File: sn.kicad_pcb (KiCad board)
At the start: 2 copper layers, 70.5 x 74.3 mm, 47 parts, among them J1 220V, J2 Load, J3 USB_C_Receptacle_USB2.0_16P, J4 Conn_02x03, Q1 BTB16-600B, Q2 BC847B, SW1 RESET, SW2 BOOT, U1 LTV-814, U2 ESP32-S3-WROOM-1, U3 MOC3052M, U5 USBLC6-2SC6, U6 LM1117MP-3.3

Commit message: redesing pcb
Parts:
- moved H3 10.5 mm to (90.8, 42.5)
- moved J1 10.2 mm to (82.5, 43.2)
- moved C7 0.28 mm to (32.0, 40.1)
- moved C8 0.28 mm to (30.1, 40.1)
- moved R7 0.19 mm to (37.7, 59.7)
- turned R2 to 0 degrees
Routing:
- net GND: track 268.2 -> 25.2 mm, vias 91 -> 77
- net Net-(J2-Pin_2): track 95.9 -> 81.0 mm, vias 0 -> 2
- net /AC_N: track 90.8 -> 78.0 mm
- net /AC_L: track 141.1 -> 135.1 mm
- removed copper zone on B.Cu, net /AC_L

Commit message: add ASM
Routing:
- net /AC_N: track 78.0 -> 74.2 mm
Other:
- board text added: "Вікторія Михайлова Група ТРМ-12"

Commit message: remove l1 l2 d4 d2
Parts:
- removed D2, D4: ESD3.3, Diode_SMD:D_SOD-923
- removed L1, L2: 220Ohm, PCM_SparkFun-Capacitor:C_0603_1608Metric
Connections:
- D3 pad 2: Net-(D3-A) -> Net-(C2-+)
- F1 pad 2: Net-(F1-Pad2) -> Net-(D1-A)
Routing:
- net Net-(C2-+): track 63.3 -> 69.5 mm
- net Net-(D3-A): track 4.94 -> 0.00 mm
- net Net-(D1-A): track 4.81 -> 9.08 mm
- net Net-(F1-Pad2): track 2.54 -> 0.00 mm
- net /ESP_IO0: track 38.3 -> 35.9 mm

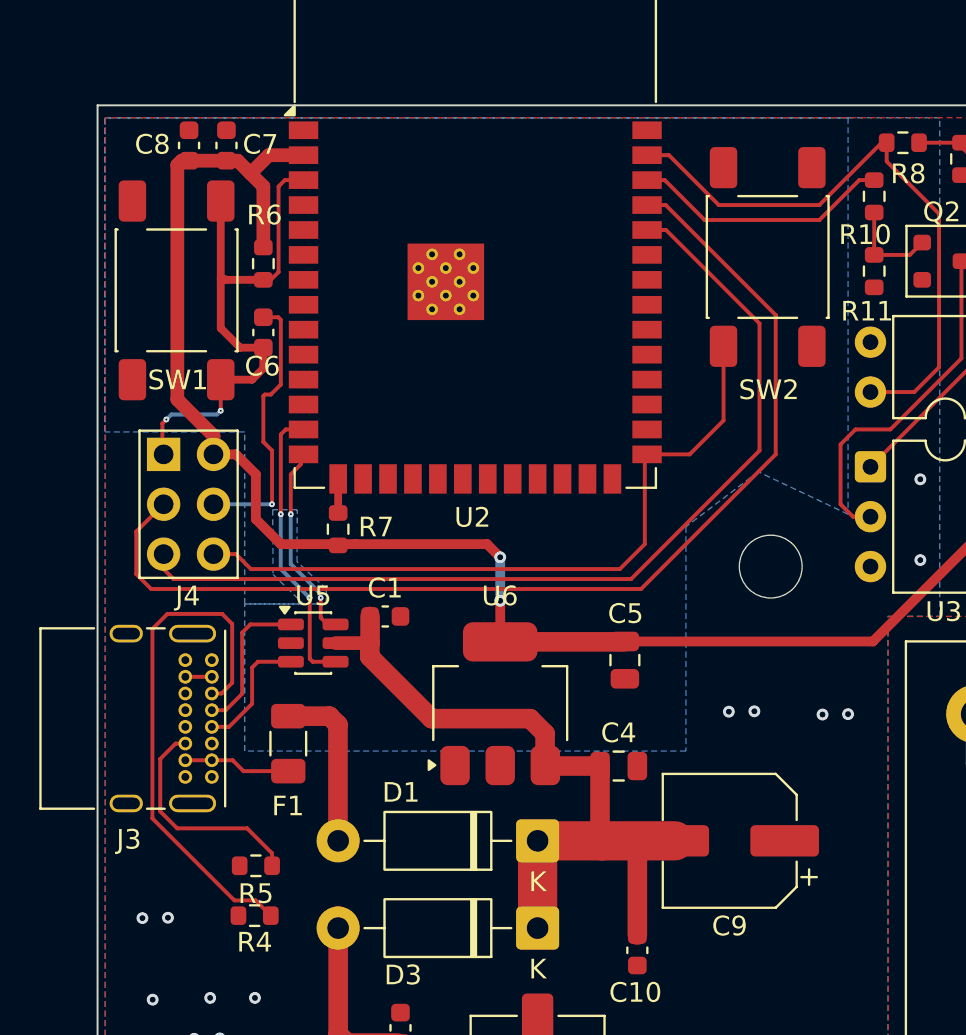
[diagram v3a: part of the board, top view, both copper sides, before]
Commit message: return tht type-c
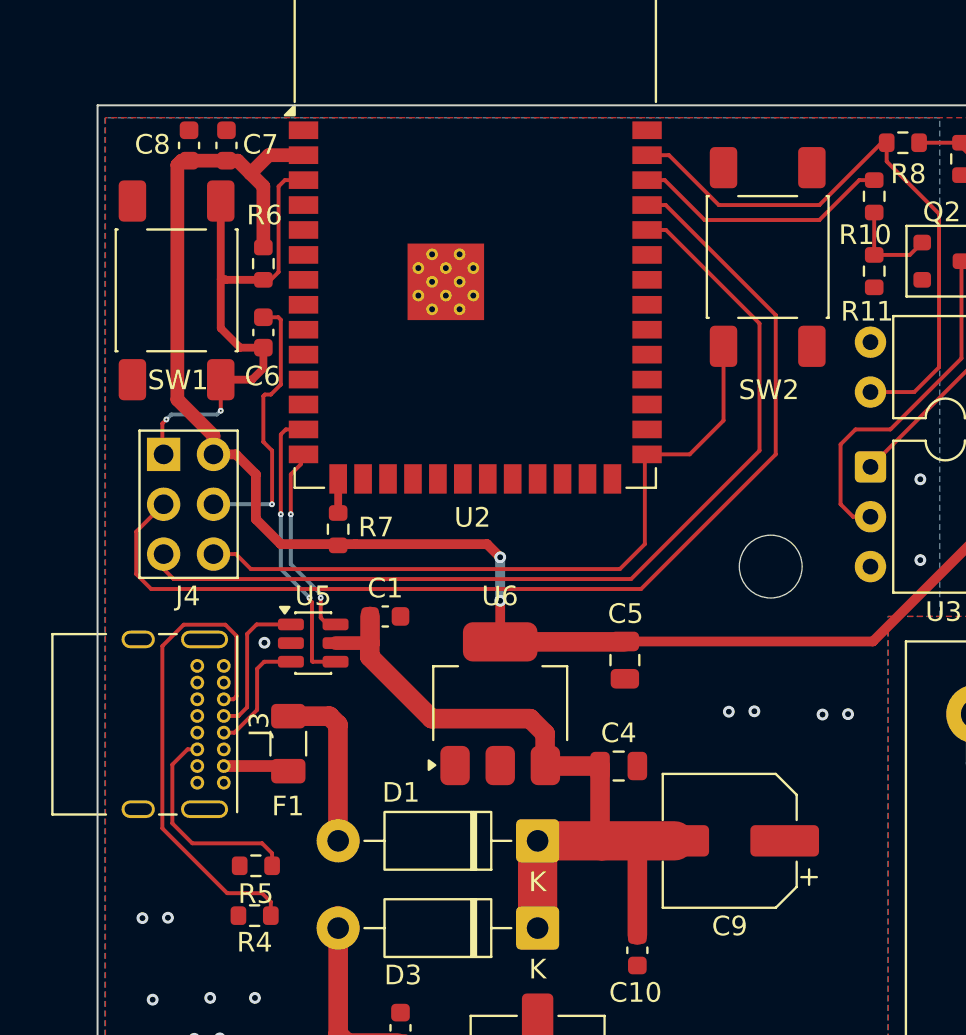
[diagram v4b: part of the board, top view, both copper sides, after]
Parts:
- moved J3 0.68 mm to (31.8, 66.7)
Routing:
- net Net-(F1-Pad1): track 6.97 -> 3.89 mm
- net /CC1: track 26.6 -> 25.3 mm
- net GND: track 25.2 -> 24.2 mm, vias 77 -> 78
- net /CC2: track 11.5 -> 10.9 mm
- net /D-: track 6.65 -> 6.14 mm

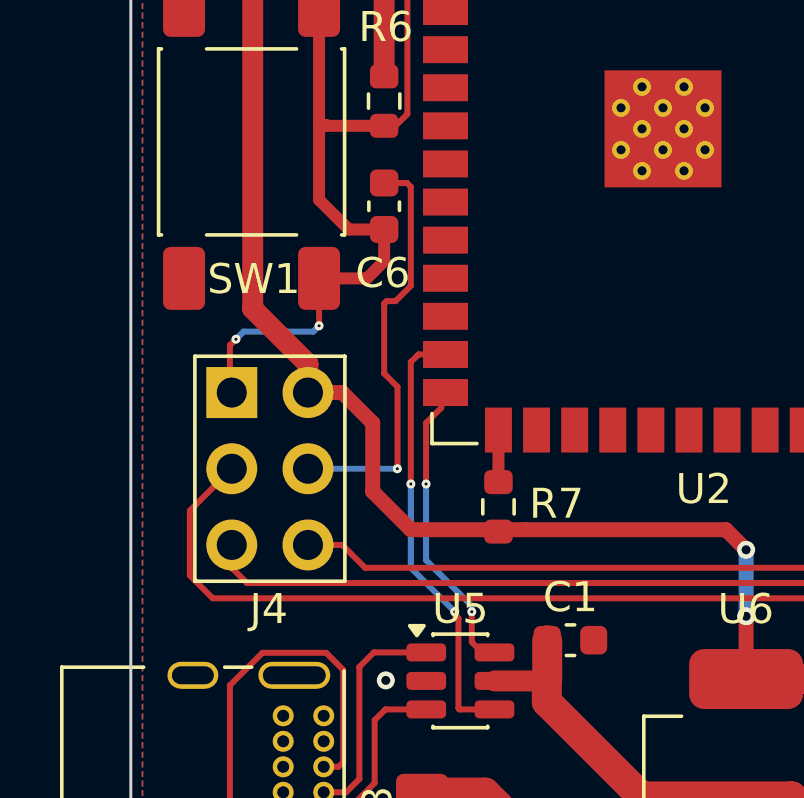
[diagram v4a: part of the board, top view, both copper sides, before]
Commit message: fix according review from JLCPCB
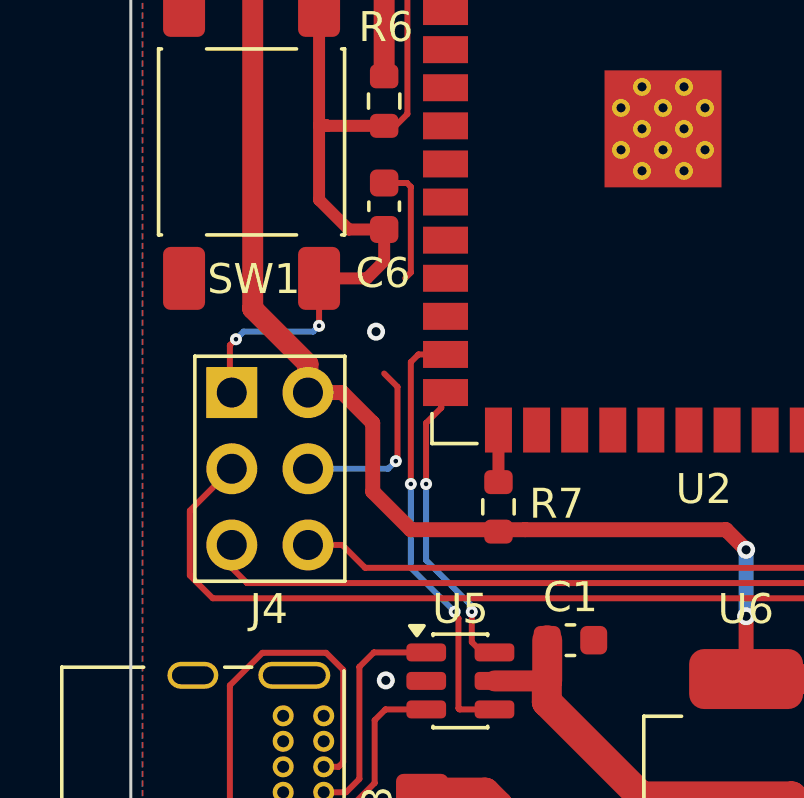
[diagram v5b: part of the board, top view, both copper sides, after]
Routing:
- net GND: track 24.2 -> 20.4 mm, vias 78 -> 79
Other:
- board text added: "Вікторія Михайлова Група ТРМ-12 2026"
- board text removed: "Вікторія Михайлова Група ТРМ-12"
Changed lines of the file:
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@@
 		(tags "ACDC-Converter 5W   Meanwell IRM-05")
 		(property "Reference" "PS1"
-			(at 41.0925 -12.925 180)
+			(at 41.0925 -12.925 0)
 			(layer "F.SilkS")
 			(effects
@@
 		)
 		(embedded_fonts no)
-		(model "${KICAD9_3DMODEL_DIR}/Converter_ACDC.3dshapes/Converter_ACDC_MeanWell_IRM-05-xx_THT.step"
+		(model "${KIPRJMOD}/TMPS 15-105--3DModel-STEP-1.STEP"
 			(offset
-				(xyz 0 0 0)
+				(xyz 20 -1.5 0)
 			)
 			(scale
@@
 			)
 			(rotate
-				(xyz 0 0 0)
+				(xyz -90 -0 90)
 			)
 		)
@@
 		(layer "Edge.Cuts")
 	)
-	(gr_text "Вікторія\nМихайлова\nГрупа ТРМ-12"
-		(at 82.7 100 270)
+	(gr_text "Вікторія\nМихайлова\nГрупа ТРМ-12\n2026"
+		(at 81.9 100 270)
 		(layer "B.SilkS")
 		(effects
@@
 	)
 	(segment
-		(start 34.2845 58.42)
-		(end 34.2845 58.3455)
-		(width 0.2)
-		(layer "F.Cu")
-		(net 7)
-	)
-	(segment
 		(start 70.125 105.939)
 		(end 64.262 100.076)
@@
 	)
 	(segment
-		(start 34.29 58.34)
-		(end 34.29 55.6895)
-		(width 0.2)
-		(layer "F.Cu")
-		(net 7)
-	)
-	(segment
-		(start 33.8455 48.895)
-		(end 34.6075 48.895)
+		(start 34.29 55.6895)
+		(end 33.8455 55.245)
 		(width 0.2)
 		(layer "F.Cu")
@@
 	)
 	(segment
-		(start 34.29 55.6895)
-		(end 33.8455 55.245)
+		(start 34.7345 49.022)
+		(end 34.6075 48.895)
 		(width 0.2)
 		(layer "F.Cu")
@@
 	)
 	(segment
-		(start 34.7345 52.324)
-		(end 34.2265 52.832)
+		(start 34.2345 58.166)
+		(end 34.29 58.1105)
 		(width 0.2)
 		(layer "F.Cu")
@@
 	)
 	(segment
-		(start 70.125 107.6075)
-		(end 70.125 105.939)
-		(width 2)
-		(layer "F.Cu")
-		(net 7)
-	)
-	(segment
-		(start 33.8455 55.245)
-		(end 33.8455 52.91)
+		(start 34.29 58.1105)
+		(end 34.29 55.6895)
 		(width 0.2)
 		(layer "F.Cu")
@@
 	)
 	(segment
-		(start 70.104 107.6285)
-		(end 70.125 107.6075)
-		(width 2)
+		(start 34.7345 51.8795)
+		(end 34.7345 49.022)
+		(width 0.2)
 		(layer "F.Cu")
 		(net 7)
 	)
 	(segment
-		(start 34.2265 52.832)
-		(end 33.9235 52.832)
+		(start 34.6075 48.895)
+		(end 33.8455 48.895)
 		(width 0.2)
 		(layer "F.Cu")
@@
 	(segment
 		(start 70.125 107.6075)
-		(end 70.125 107.675)
+		(end 70.125 105.939)
 		(width 2)
 		(layer "F.Cu")
@@
 	)
 	(segment
-		(start 34.6075 48.895)
-		(end 34.7345 49.022)
-		(width 0.2)
+		(start 70.104 107.6285)
+		(end 70.125 107.6075)
+		(width 2)
 		(layer "F.Cu")
 		(net 7)
 	)
 	(segment
-		(start 34.2845 58.3455)
-		(end 34.29 58.34)
-		(width 0.2)
+		(start 70.125 107.6075)
+		(end 70.125 107.675)
+		(width 2)
 		(layer "F.Cu")
 		(net 7)
@@
 	)
 	(segment
-		(start 33.9235 52.832)
-		(end 33.8455 52.91)
-		(width 0.2)
-		(layer "F.Cu")
-		(net 7)
-	)
-	(segment
-		(start 34.7345 49.022)
-		(end 34.7345 52.324)
+		(start 34.544 52.07)
+		(end 34.7345 51.8795)
 		(width 0.2)
 		(layer "F.Cu")
@@
 	)
 	(via micro
-		(at 34.2845 58.42)
-		(size 0.3)
-		(drill 0.1)
+		(at 34.2345 58.166)
+		(size 0.4)
+		(drill 0.15)
 		(layers "F.Cu" "B.Cu")
 		(net 7)
@@
 	)
 	(via
+		(at 33.575 53.85)
+		(size 0.6)
+		(drill 0.3)
+		(layers "F.Cu" "B.Cu")
+		(free yes)
+		(net 7)
+	)
+	(via
 		(at 51.9684 95.9612)
 		(size 0.6)
@@
 	)
 	(segment
+		(start 33.9805 58.42)
+		(end 34.2345 58.166)
+		(width 0.2)
+		(layer "B.Cu")
+		(net 7)
+	)
+	(segment
 		(start 31.3055 58.42)
-		(end 34.2845 58.42)
+		(end 33.9805 58.42)
 		(width 0.2)
 		(layer "B.Cu")
@@
 	(via micro
 		(at 28.9052 54.102)
-		(size 0.3)
-		(drill 0.1)
+		(size 0.4)
+		(drill 0.15)
 		(layers "F.Cu" "B.Cu")
 		(net 8)
@@
 	(via micro
 		(at 31.6755 53.6558)
-		(size 0.3)
-		(drill 0.1)
+		(size 0.4)
+		(drill 0.15)
 		(layers "F.Cu" "B.Cu")
 		(net 8)
@@
 	(via micro
 		(at 35.2425 58.928)
-		(size 0.3)
-		(drill 0.1)
+		(size 0.4)
+		(drill 0.15)
 		(layers "F.Cu" "B.Cu")
 		(net 49)
@@
 	(via micro
 		(at 36.7665 63.188)
-		(size 0.3)
-		(drill 0.1)
+		(size 0.4)
+		(drill 0.15)
 		(layers "F.Cu" "B.Cu")
 		(net 49)
@@
 	(via micro
 		(at 34.7345 58.928)
-		(size 0.3)
-		(drill 0.1)
+		(size 0.4)
+		(drill 0.15)
 		(layers "F.Cu" "B.Cu")
 		(net 52)
@@
 	(via micro
 		(at 36.19625 63.188)
-		(size 0.3)
-		(drill 0.1)
+		(size 0.4)
+		(drill 0.15)
 		(layers "F.Cu" "B.Cu")
 		(net 52)
